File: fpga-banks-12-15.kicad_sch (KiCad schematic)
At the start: 1 part, among them U1 XC7K410T-2FFG900I

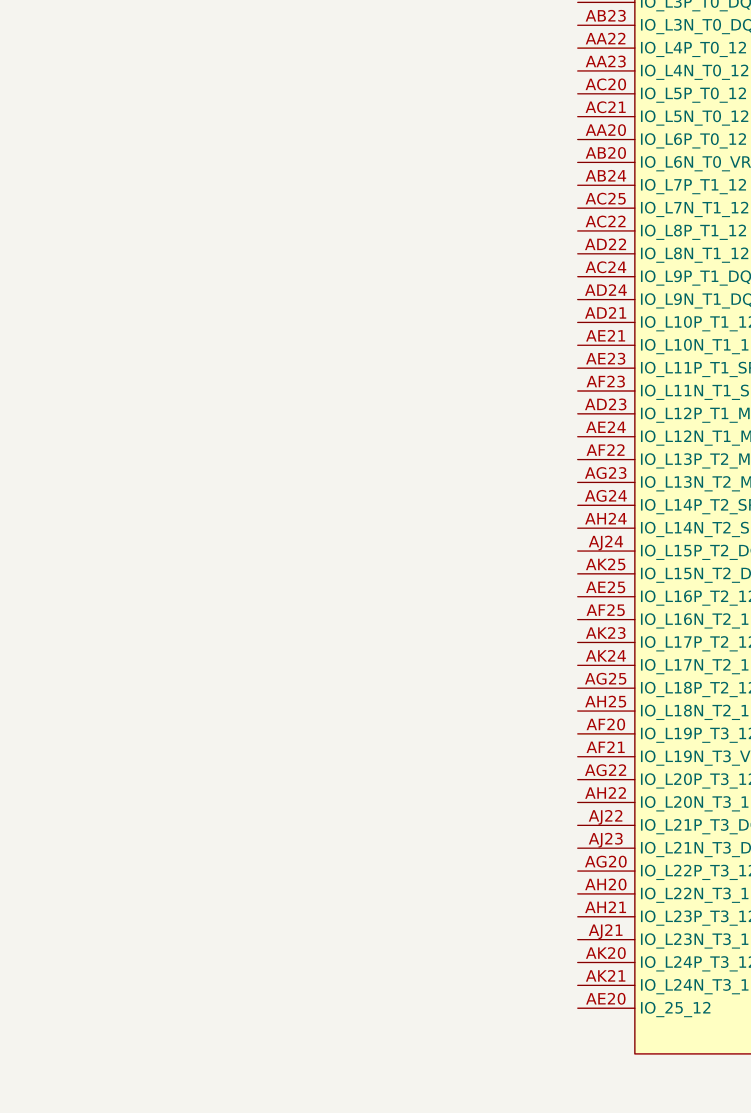
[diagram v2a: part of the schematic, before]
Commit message: Add CW-20PIN connector and connect it to FPGA
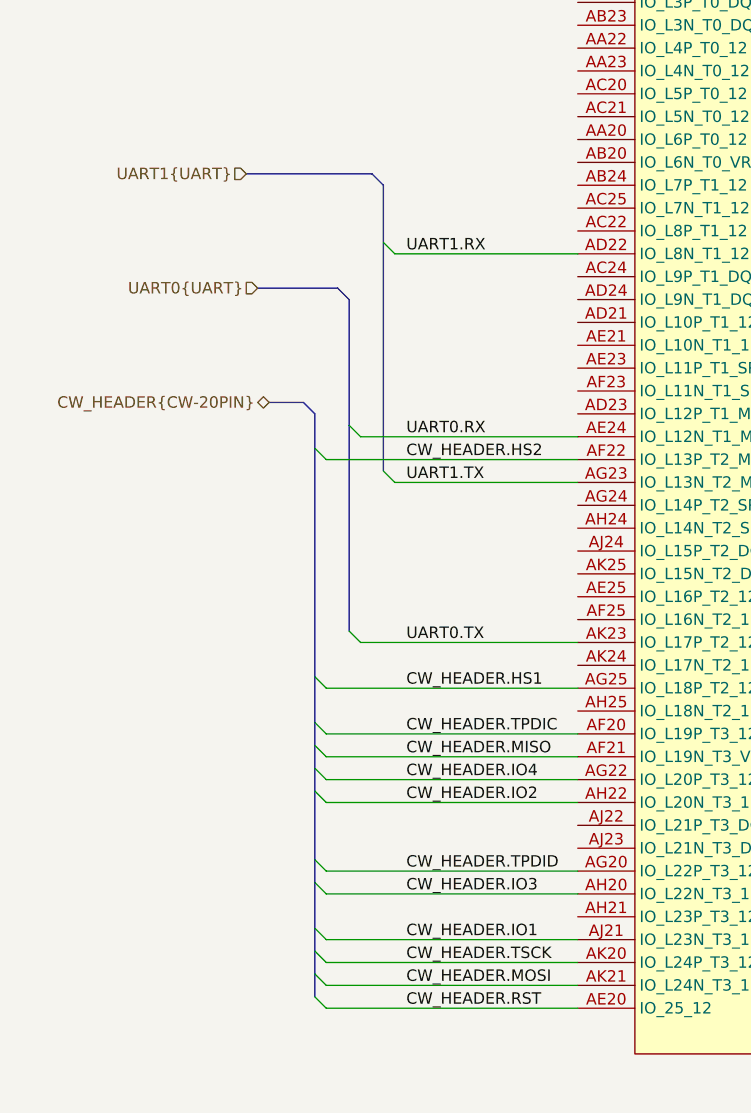
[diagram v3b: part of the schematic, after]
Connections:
- net UART1.RX: now reaches U1.AD22 (IO_L8N_T1_12)
- net CW_HEADER.RST: now reaches U1.AE20 (IO_25_12)
- net UART0.RX: now reaches U1.AE24 (IO_L12N_T1_MRCC_12)
- net CW_HEADER.TPDIC: now reaches U1.AF20 (IO_L19P_T3_12)
- net CW_HEADER.MISO: now reaches U1.AF21 (IO_L19N_T3_VREF_12)
- net CW_HEADER.HS2: now reaches U1.AF22 (IO_L13P_T2_MRCC_12)
- net CW_HEADER.TPDID: now reaches U1.AG20 (IO_L22P_T3_12)
- net CW_HEADER.IO4: now reaches U1.AG22 (IO_L20P_T3_12)
- net UART1.TX: now reaches U1.AG23 (IO_L13N_T2_MRCC_12)
- net CW_HEADER.HS1: now reaches U1.AG25 (IO_L18P_T2_12)
- net CW_HEADER.IO3: now reaches U1.AH20 (IO_L22N_T3_12)
- net CW_HEADER.IO2: now reaches U1.AH22 (IO_L20N_T3_12)
- net CW_HEADER.IO1: now reaches U1.AJ21 (IO_L23N_T3_12)
- net CW_HEADER.TSCK: now reaches U1.AK20 (IO_L24P_T3_12)
- net CW_HEADER.MOSI: now reaches U1.AK21 (IO_L24N_T3_12)
- net UART0.TX: now reaches U1.AK23 (IO_L17P_T2_12)
